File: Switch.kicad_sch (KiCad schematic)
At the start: 3 parts, among them SW1001 SW_Push

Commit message: update plików
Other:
- company: (none) -> Szymon Przybył
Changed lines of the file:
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@@
 (kicad_sch (version 20211123) (generator eeschema)
   (paper "A4")
+  (title_block
+    (date "2023-02-20")
+    (company "Szymon Przybył")
+  )
   (junction (at 117.475 94.615) (diameter 0) (color 0 0 0 0)
   )

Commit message: schematic update after meeting
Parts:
- R1001: value R -> 100R
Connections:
- net Switch: now also C1001.1
- net at R1001.2, SW1001.1: no longer C1001.1
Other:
- note added: "złe footprinty"
- moved on the sheet: R1001
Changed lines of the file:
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@@
     (company "Szymon Przybył")
   )
-  (junction (at 117.475 94.615) (diameter 0) (color 0 0 0 0)
+  (junction (at 106.68 94.615) (diameter 0) (color 0 0 0 0)
   )
-  (wire (pts (xy 112.395 94.615) (xy 117.475 94.615))
-    (stroke (width 0) (type default) (color 0 0 0 0))
-  )
-  (wire (pts (xy 117.475 94.615) (xy 122.555 94.615))
+  (wire (pts (xy 118.11 94.615) (xy 122.555 94.615))
     (stroke (width 0) (type default) (color 0 0 0 0))
   )
@@
     (stroke (width 0) (type default) (color 0 0 0 0))
   )
-  (wire (pts (xy 117.475 106.045) (xy 117.475 109.855))
+  (wire (pts (xy 106.68 94.615) (xy 110.49 94.615))
+    (stroke (width 0) (type default) (color 0 0 0 0))
+  )
+  (wire (pts (xy 106.68 106.045) (xy 106.68 109.855))
+    (stroke (width 0) (type default) (color 0 0 0 0))
+  )
+  (wire (pts (xy 106.68 94.615) (xy 106.68 98.425))
     (stroke (width 0) (type default) (color 0 0 0 0))
   )
@@
     (stroke (width 0) (type default) (color 0 0 0 0))
   )
-  (wire (pts (xy 96.52 94.615) (xy 104.775 94.615))
+  (wire (pts (xy 96.52 94.615) (xy 106.68 94.615))
     (stroke (width 0) (type default) (color 0 0 0 0))
   )
-  (wire (pts (xy 117.475 94.615) (xy 117.475 98.425))
-    (stroke (width 0) (type default) (color 0 0 0 0))
+  (text "złe footprinty" (at 158.115 100.33 0)
+    (effects (font (size 1.27 1.27)) (justify left bottom))
   )
   (hierarchical_label "Switch" (shape input) (at 96.52 94.615 180)
     (effects (font (size 1.27 1.27)) (justify right))
   )
-  (symbol (lib_id "Device:R") (at 108.585 94.615 90) (unit 1)
+  (symbol (lib_id "Device:R") (at 114.3 94.615 90) (unit 1)
     (in_bom yes) (on_board yes) (fields_autoplaced)
-    (property "Reference" "R1001" (id 0) (at 108.585 88.265 90))
-    (property "Value" "R" (id 1) (at 108.585 90.805 90))
-    (property "Footprint" "Resistor_THT:R_Axial_DIN0204_L3.6mm_D1.6mm_P7.62mm_Horizontal" (id 2) (at 108.585 96.393 90)
+    (property "Reference" "R1001" (id 0) (at 114.3 88.9 90))
+    (property "Value" "100R" (id 1) (at 114.3 91.44 90))
+    (property "Footprint" "Resistor_THT:R_Axial_DIN0204_L3.6mm_D1.6mm_P7.62mm_Horizontal" (id 2) (at 114.3 96.393 90)
       (effects (font (size 1.27 1.27)) hide)
     )
-    (property "Datasheet" "~" (id 3) (at 108.585 94.615 0)
+    (property "Datasheet" "~" (id 3) (at 114.3 94.615 0)
       (effects (font (size 1.27 1.27)) hide)
     )
@@
     (pin "1")
   )
-  (symbol (lib_id "Device:C") (at 117.475 102.235 0) (unit 1)
-    (in_bom yes) (on_board yes) (fields_autoplaced)
-    (property "Reference" "C1001" (id 0) (at 120.65 100.9649 0)
-      (effects (font (size 1.27 1.27)) (justify left))
-    )
-    (property "Value" "100nF" (id 1) (at 120.65 103.5049 0)
-      (effects (font (size 1.27 1.27)) (justify left))
-    )
-    (property "Footprint" "Capacitor_THT:C_Disc_D3.0mm_W1.6mm_P2.50mm" (id 2) (at 118.4402 106.045 0)
-      (effects (font (size 1.27 1.27)) hide)
-    )
-    (property "Datasheet" "~" (id 3) (at 117.475 102.235 0)
-      (effects (font (size 1.27 1.27)) hide)
-    )
-    (pin "1")
-    (pin "2")
-  )
   (symbol (lib_id "Switch:SW_Push") (at 127.635 94.615 0) (unit 1)
     (in_bom yes) (on_board yes) (fields_autoplaced)
@@
     (pin "2")
   )
-  (symbol (lib_id "power:GND") (at 117.475 109.855 0) (mirror y) (unit 1)
+  (symbol (lib_id "Device:C") (at 106.68 102.235 0) (unit 1)
     (in_bom yes) (on_board yes) (fields_autoplaced)
-    (property "Reference" "#PWR01001" (id 0) (at 117.475 116.205 0)
+    (property "Reference" "C1001" (id 0) (at 109.855 100.9649 0)
+      (effects (font (size 1.27 1.27)) (justify left))
+    )
+    (property "Value" "100nF" (id 1) (at 109.855 103.5049 0)
+      (effects (font (size 1.27 1.27)) (justify left))
+    )
+    (property "Footprint" "Capacitor_THT:C_Disc_D3.0mm_W1.6mm_P2.50mm" (id 2) (at 107.6452 106.045 0)
       (effects (font (size 1.27 1.27)) hide)
     )
-    (property "Value" "GND" (id 1) (at 117.475 114.935 0))
-    (property "Footprint" "" (id 2) (at 117.475 109.855 0)
+    (property "Datasheet" "~" (id 3) (at 106.68 102.235 0)
       (effects (font (size 1.27 1.27)) hide)
     )
-    (property "Datasheet" "" (id 3) (at 117.475 109.855 0)
+    (pin "1")
+    (pin "2")
+  )
+  (symbol (lib_id "power:GND") (at 106.68 109.855 0) (mirror y) (unit 1)
+    (in_bom yes) (on_board yes) (fields_autoplaced)
+    (property "Reference" "#PWR01001" (id 0) (at 106.68 116.205 0)
       (effects (font (size 1.27 1.27)) hide)
     )
+    (property "Value" "GND" (id 1) (at 106.68 114.935 0))
+    (property "Footprint" "" (id 2) (at 106.68 109.855 0)
+      (effects (font (size 1.27 1.27)) hide)
+    )
+    (property "Datasheet" "" (id 3) (at 106.68 109.855 0)
+      (effects (font (size 1.27 1.27)) hide)
+    )

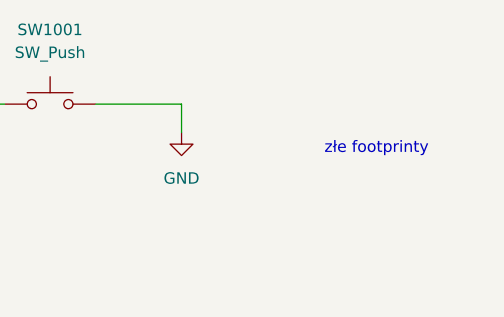
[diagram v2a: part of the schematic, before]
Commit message: layout update moved power section to the bottom of the board, ibom generated, changed footprint for switches
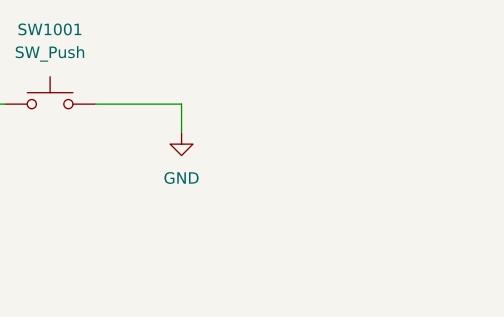
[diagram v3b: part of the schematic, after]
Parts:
- SW1001: footprint Tact Switch 3x6 mm 5 mm THT:DIP-2_236_ELL -> Tact Switch 6x6 mm 5 mm THT:Tact Switch 6x6mm 5mm
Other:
- note removed: "złe footprinty"

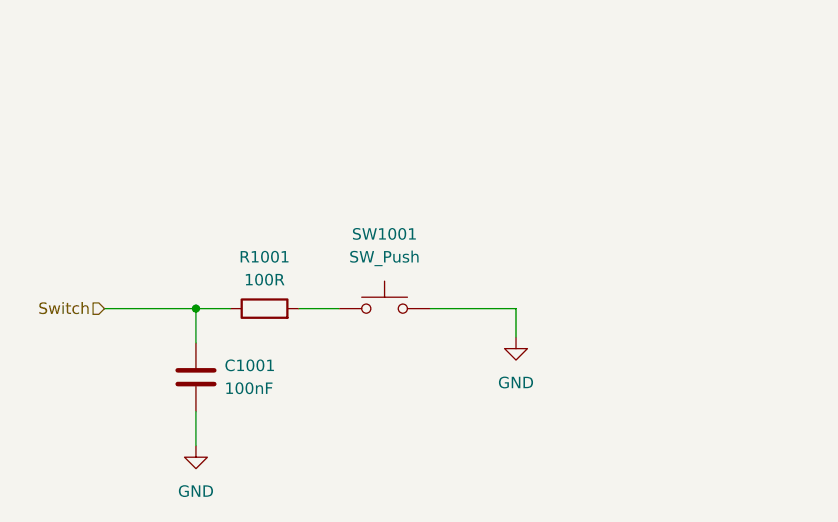
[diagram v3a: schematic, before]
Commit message: [FEAT] Zaktualizowano układ do debauncing
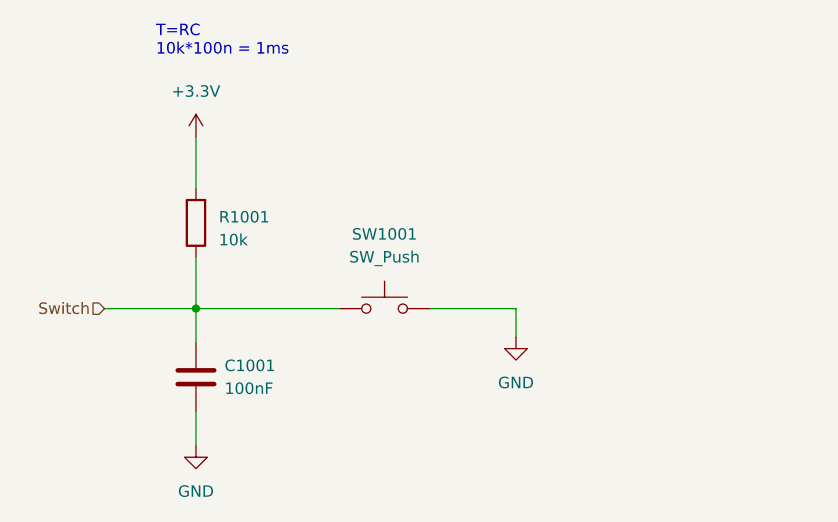
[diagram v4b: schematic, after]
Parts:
- R1001: value 100R -> 10k
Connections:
- net Switch: now also SW1001.1
- net +3.3V: now reaches R1001.2
- net +3.3V: no longer SW1001.1
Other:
- note added: "T=RC 10k*100n = 1ms"
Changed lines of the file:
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@@
   (junction (at 106.68 94.615) (diameter 0) (color 0 0 0 0)
-  )
-  (wire (pts (xy 118.11 94.615) (xy 122.555 94.615))
-    (stroke (width 0) (type default))
   )
   (wire (pts (xy 142.24 94.615) (xy 142.24 97.79))
     (stroke (width 0) (type default))
   )
-  (wire (pts (xy 106.68 94.615) (xy 110.49 94.615))
+  (wire (pts (xy 106.68 94.615) (xy 122.555 94.615))
     (stroke (width 0) (type default))
   )
@@
     (stroke (width 0) (type default))
   )
+  (wire (pts (xy 106.68 75.565) (xy 106.68 81.28))
+    (stroke (width 0) (type default))
+  )
+  (wire (pts (xy 106.68 88.9) (xy 106.68 94.615))
+    (stroke (width 0) (type default))
+  )
+  (text "T=RC\n10k*100n = 1ms" (at 102.235 66.675 0)
+    (effects (font (size 1.27 1.27)) (justify left bottom))
+  )
   (hierarchical_label "Switch" (shape input) (at 96.52 94.615 180) (fields_autoplaced)
     (effects (font (size 1.27 1.27)) (justify right))
   )
-  (symbol (lib_id "Device:R") (at 114.3 94.615 90) (unit 1)
+  (symbol (lib_id "Device:R") (at 106.68 85.09 180) (unit 1)
     (in_bom yes) (on_board yes) (dnp no) (fields_autoplaced)
-    (property "Reference" "R1001" (at 114.3 88.9 90)
-      (effects (font (size 1.27 1.27)))
+    (property "Reference" "R1001" (at 109.22 84.455 0)
+      (effects (font (size 1.27 1.27)) (justify right))
     )
-    (property "Value" "100R" (at 114.3 91.44 90)
-      (effects (font (size 1.27 1.27)))
+    (property "Value" "10k" (at 109.22 86.995 0)
+      (effects (font (size 1.27 1.27)) (justify right))
     )
-    (property "Footprint" "Resistor_THT:R_Axial_DIN0204_L3.6mm_D1.6mm_P7.62mm_Horizontal" (at 114.3 96.393 90)
+    (property "Footprint" "Resistor_THT:R_Axial_DIN0204_L3.6mm_D1.6mm_P7.62mm_Horizontal" (at 108.458 85.09 90)
       (effects (font (size 1.27 1.27)) hide)
     )
-    (property "Datasheet" "~" (at 114.3 94.615 0)
+    (property "Datasheet" "~" (at 106.68 85.09 0)
       (effects (font (size 1.27 1.27)) hide)
     )
@@
         )
       )
+    )
+  )
+  (symbol (lib_id "power:+3.3V") (at 106.68 75.565 0) (unit 1)
+    (in_bom yes) (on_board yes) (dnp no) (fields_autoplaced)
+    (property "Reference" "#PWR0107" (at 106.68 79.375 0)
+      (effects (font (size 1.27 1.27)) hide)
+    )
+    (property "Value" "+3.3V" (at 106.68 70.485 0)
+      (effects (font (size 1.27 1.27)))
+    )
+    (property "Footprint" "" (at 106.68 75.565 0)
+      (effects (font (size 1.27 1.27)) hide)
+    )
+    (property "Datasheet" "" (at 106.68 75.565 0)
+      (effects (font (size 1.27 1.27)) hide)
+    )
+    (pin "1")
+    (instances
+      (project "AutkoPcb"
+        (path "/6bb4e9ec-1d99-446d-aada-1b0d10ea69f3"
+          (reference "#PWR0107") (unit 1)
+        )
+        (path "/6bb4e9ec-1d99-446d-aada-1b0d10ea69f3/95d09731-6b5e-489f-a967-d036e836aa83/1935bcae-29b1-4831-ba24-b860b7de256d"
+          (reference "#PWR01003") (unit 1)
+        )
+        (path "/6bb4e9ec-1d99-446d-aada-1b0d10ea69f3/95d09731-6b5e-489f-a967-d036e836aa83/05e74570-80bf-48e3-abfc-926ab8afd1de"
+          (reference "#PWR01103") (unit 1)
+        )
+        (path "/6bb4e9ec-1d99-446d-aada-1b0d10ea69f3/95d09731-6b5e-489f-a967-d036e836aa83/f4ff12bd-e38f-489e-8dca-c3f8d9ea1ef6"
+          (reference "#PWR01203") (unit 1)
+        )
+        (path "/6bb4e9ec-1d99-446d-aada-1b0d10ea69f3/95d09731-6b5e-489f-a967-d036e836aa83/a5c0f2e6-25cd-4265-a7d1-24afeb283314"
+          (reference "#PWR01303") (unit 1)
+        )
+      )
